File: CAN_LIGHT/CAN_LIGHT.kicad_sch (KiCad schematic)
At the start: 86 parts, among them IC1 MSPM0C1103SDDFR, J1 Conn_ARM_SWD_TagConnect_TC2030, J2 436500401, U1 TCAN334, U2 TPS76333DBVR

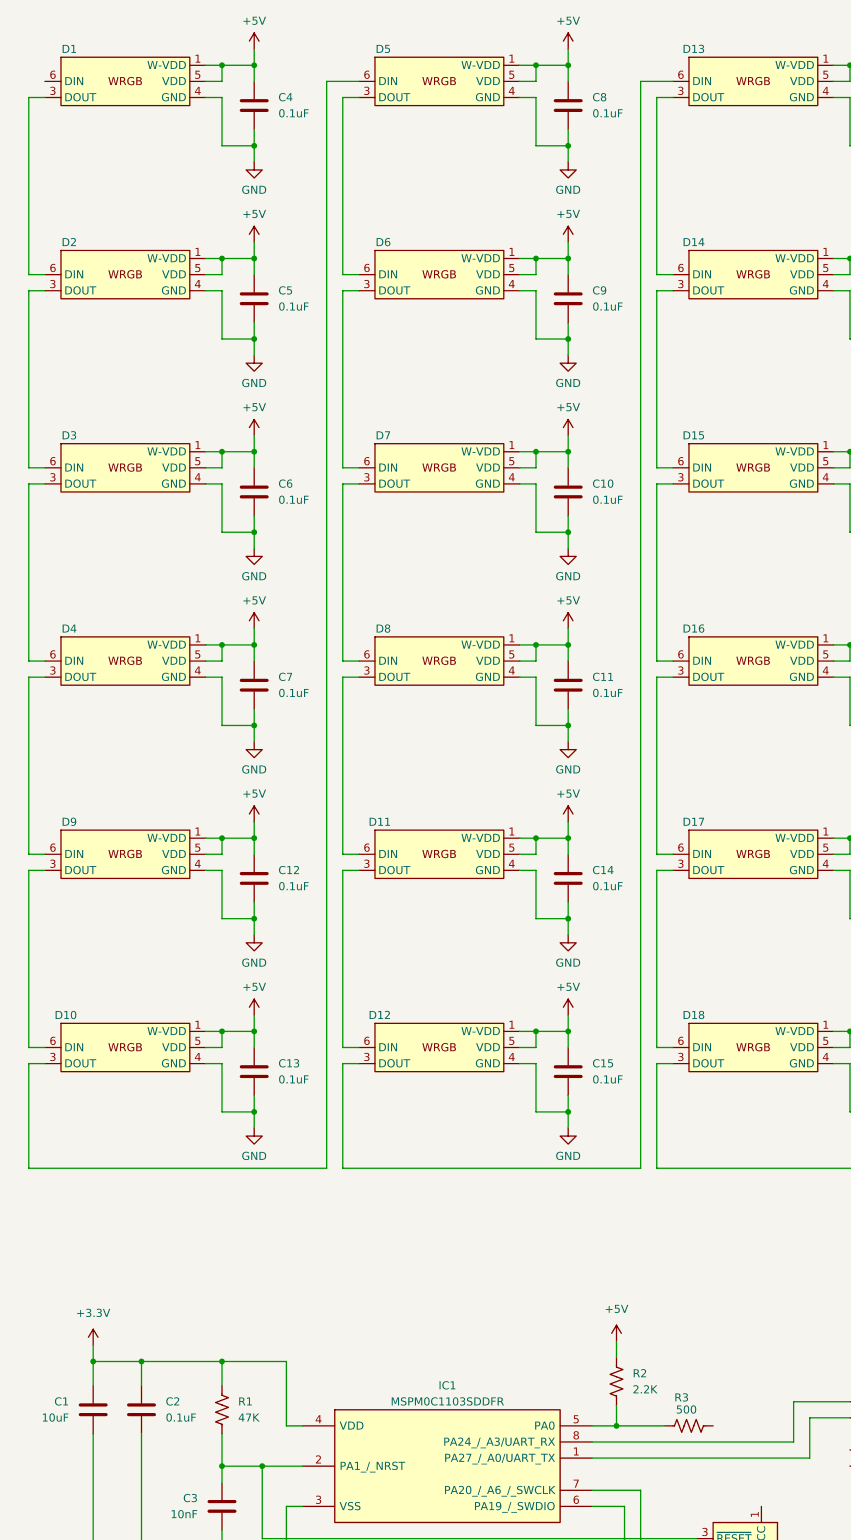
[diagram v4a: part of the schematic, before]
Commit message: Wire LEDs to MCU
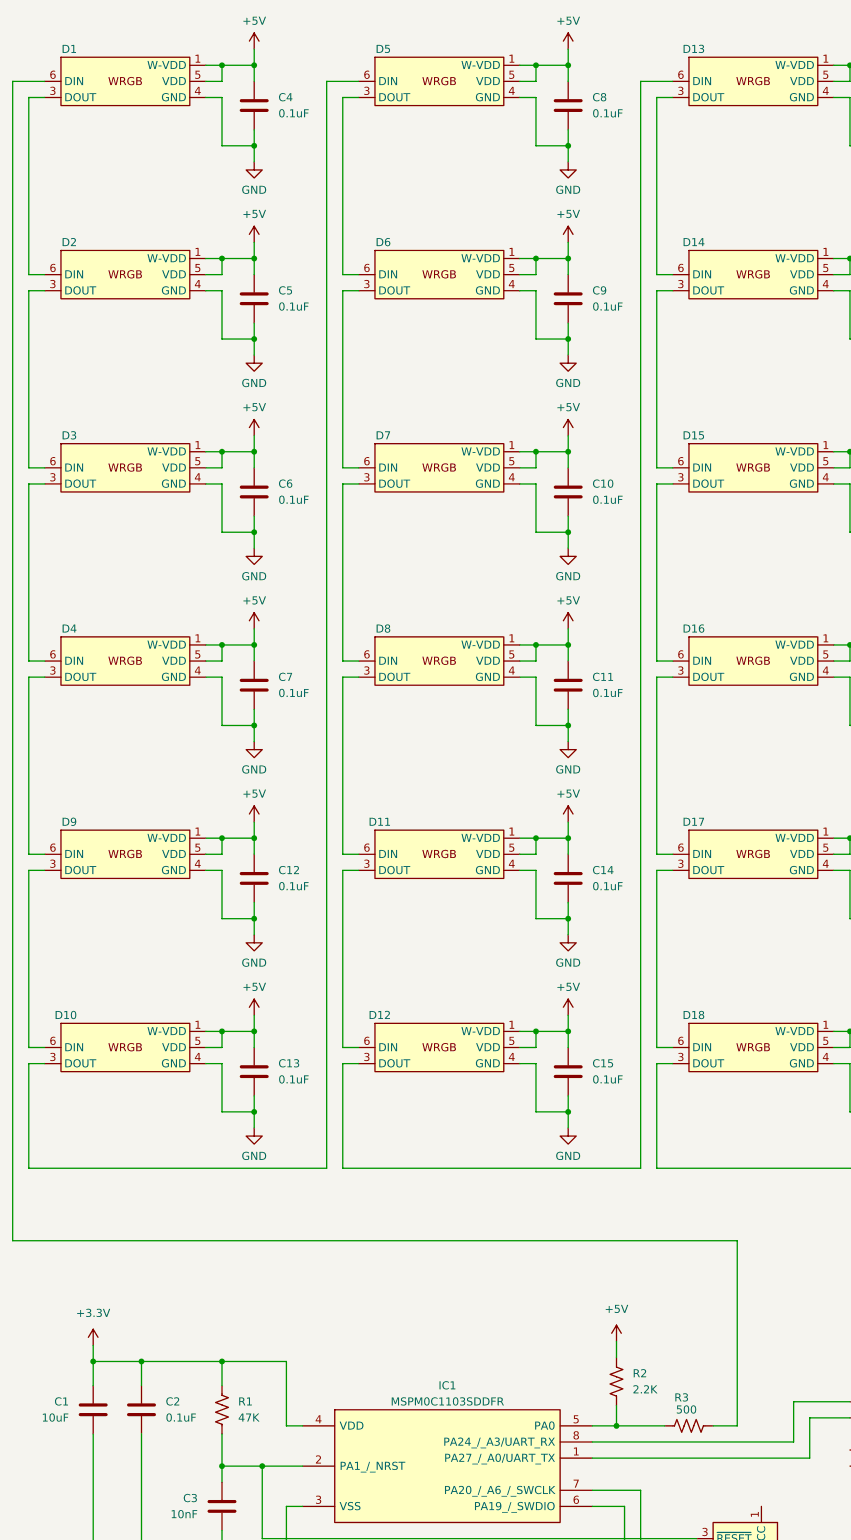
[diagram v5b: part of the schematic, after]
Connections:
- net at D1.6 (DIN): now also R3.2
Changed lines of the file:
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@@
+    (stroke (width 0) (type default))
+  )
+  (wire (pts (xy 127 236.22) (xy 130.81 236.22))
     (stroke (width 0) (type default))
   )
@@
     (stroke (width 0) (type default))
   )
+  (wire (pts (xy 130.81 236.22) (xy 130.81 207.01))
+    (stroke (width 0) (type default))
+  )
   (wire (pts (xy 104.14 143.51) (xy 99.06 143.51))
     (stroke (width 0) (type default))
@@
     (stroke (width 0) (type default))
   )
+  (wire (pts (xy 16.51 207.01) (xy 16.51 24.13))
+    (stroke (width 0) (type default))
+  )
   (wire (pts (xy 96.52 179.07) (xy 99.06 179.07))
     (stroke (width 0) (type default))
@@
     (stroke (width 0) (type default))
   )
+  (wire (pts (xy 16.51 24.13) (xy 21.59 24.13))
+    (stroke (width 0) (type default))
+  )
   (wire (pts (xy 203.2 186.69) (xy 203.2 189.23))
     (stroke (width 0) (type default))
@@
     (stroke (width 0) (type default))
   )
+  (wire (pts (xy 130.81 207.01) (xy 16.51 207.01))
+    (stroke (width 0) (type default))
+  )

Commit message: Add 12V to 5V buck converter
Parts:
- added U3: NCV891330PD50R2G, SOIC8_3P9X4P9_ONS, symbol NCV891330PD50R2G:NCV891330PD50R2G
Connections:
- net +12V: now also U3.1 (VIN)
- net +5V: now also U3.6 (VOUT)
- net GND: now also U3.4 (GND)
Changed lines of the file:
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@@
     (stroke (width 0) (type default))
   )
+  (wire (pts (xy 325.12 220.98) (xy 325.12 226.06))
+    (stroke (width 0) (type default))
+  )
   (wire (pts (xy 46.99 85.09) (xy 49.53 85.09))
     (stroke (width 0) (type default))
@@
     (stroke (width 0) (type default))
   )
+  (wire (pts (xy 386.08 218.44) (xy 386.08 208.28))
+    (stroke (width 0) (type default))
+  )
   (wire (pts (xy 124.46 254) (xy 55.88 254))
     (stroke (width 0) (type default))
@@
     (stroke (width 0) (type default))
   )
+  (wire (pts (xy 325.12 213.36) (xy 325.12 208.28))
+    (stroke (width 0) (type default))
+  )
   (wire (pts (xy 195.58 176.53) (xy 198.12 176.53))
     (stroke (width 0) (type default))
@@
     (stroke (width 0) (type default))
   )
+  (wire (pts (xy 330.2 213.36) (xy 325.12 213.36))
+    (stroke (width 0) (type default))
+  )
   (wire (pts (xy 252.73 140.97) (xy 252.73 143.51))
     (stroke (width 0) (type default))
@@
     (stroke (width 0) (type default))
   )
+  (wire (pts (xy 330.2 220.98) (xy 325.12 220.98))
+    (stroke (width 0) (type default))
+  )
   (wire (pts (xy 134.62 269.24) (xy 134.62 273.05))
     (stroke (width 0) (type default))
@@
     (stroke (width 0) (type default))
   )
+  (wire (pts (xy 370.84 218.44) (xy 386.08 218.44))
+    (stroke (width 0) (type default))
+  )
   (wire (pts (xy 153.67 113.03) (xy 153.67 115.57))
     (stroke (width 0) (type default))
@@
     )
   )
+  (symbol (lib_id "power:+5V") (at 386.08 208.28 0) (unit 1)
+    (in_bom yes) (on_board yes) (dnp no) (fields_autoplaced)
+    (property "Reference" "#PWR088" (at 386.08 212.09 0)
+      (effects (font (size 1.27 1.27)) hide)
+    )
+    (property "Value" "+5V" (at 386.08 203.2 0)
+      (effects (font (size 1.27 1.27)))
+    )
+    (property "Footprint" "" (at 386.08 208.28 0)
+      (effects (font (size 1.27 1.27)) hide)
+    )
+    (property "Datasheet" "" (at 386.08 208.28 0)
+      (effects (font (size 1.27 1.27)) hide)
+    )
+    (pin "1")
+    (instances
+      (project "CAN_LIGHT"
+        (path "/d4f25219-6cef-4e47-aded-6c41d03d24e2"
+          (reference "#PWR088") (unit 1)
+        )
+      )
+    )
+  )
   (symbol (lib_id "LED:IN-PI4818QAS5R5G5BPW") (at 24.13 27.94 0) (unit 1)
     (in_bom yes) (on_board yes) (dnp no)
@@
     )
   )
+  (symbol (lib_id "NCV891330PD50R2G:NCV891330PD50R2G") (at 330.2 213.36 0) (unit 1)
+    (in_bom yes) (on_board yes) (dnp no) (fields_autoplaced)
+    (property "Reference" "U3" (at 350.52 203.2 0)
+      (effects (font (size 1.524 1.524)))
+    )
+    (property "Value" "NCV891330PD50R2G" (at 350.52 205.74 0)
+      (effects (font (size 1.524 1.524)))
+    )
+    (property "Footprint" "SOIC8_3P9X4P9_ONS" (at 330.2 213.36 0)
+      (effects (font (size 1.27 1.27) italic) hide)
+    )
+    (property "Datasheet" "NCV891330PD50R2G" (at 330.2 213.36 0)
+      (effects (font (size 1.27 1.27) italic) hide)
+    )
+    (pin "1")
+    (pin "2")
+    (pin "3")
+    (pin "4")
+    (pin "5")
+    (pin "6")
+    (pin "7")
+    (pin "8")
+    (instances
+      (project "CAN_LIGHT"
+        (path "/d4f25219-6cef-4e47-aded-6c41d03d24e2"
+          (reference "U3") (unit 1)
+        )
+      )
+    )
+  )
   (symbol (lib_id "LED:IN-PI4818QAS5R5G5BPW") (at 271.78 180.34 0) (unit 1)
     (in_bom yes) (on_board yes) (dnp no)
@@
     )
   )
+  (symbol (lib_id "power:+12V") (at 325.12 208.28 0) (unit 1)
+    (in_bom yes) (on_board yes) (dnp no) (fields_autoplaced)
+    (property "Reference" "#PWR086" (at 325.12 212.09 0)
+      (effects (font (size 1.27 1.27)) hide)
+    )
+    (property "Value" "+12V" (at 325.12 203.2 0)
+      (effects (font (size 1.27 1.27)))
+    )
+    (property "Footprint" "" (at 325.12 208.28 0)
+      (effects (font (size 1.27 1.27)) hide)
+    )
+    (property "Datasheet" "" (at 325.12 208.28 0)
+      (effects (font (size 1.27 1.27)) hide)
+    )
+    (pin "1")
+    (instances
+      (project "CAN_LIGHT"
+        (path "/d4f25219-6cef-4e47-aded-6c41d03d24e2"
+          (reference "#PWR086") (unit 1)
+        )
+      )
+    )
+  )
   (symbol (lib_id "power:GND") (at 302.26 97.79 0) (mirror y) (unit 1)
     (in_bom yes) (on_board yes) (dnp no) (fields_autoplaced)
@@
         )
       )
+    )
+  )
+  (symbol (lib_id "power:GND") (at 325.12 226.06 0) (unit 1)
+    (in_bom yes) (on_board yes) (dnp no) (fields_autoplaced)
+    (property "Reference" "#PWR087" (at 325.12 232.41 0)
+      (effects (font (size 1.27 1.27)) hide)
+    )
+    (property "Value" "GND" (at 325.12 231.14 0)
+      (effects (font (size 1.27 1.27)))
+    )
+    (property "Footprint" "" (at 325.12 226.06 0)
+      (effects (font (size 1.27 1.27)) hide)
+    )
+    (property "Datasheet" "" (at 325.12 226.06 0)
+      (effects (font (size 1.27 1.27)) hide)
+    )
+    (pin "1")
+    (instances
+      (project "CAN_LIGHT"
+        (path "/d4f25219-6cef-4e47-aded-6c41d03d24e2"
+          (reference "#PWR087") (unit 1)
+        )
+      )

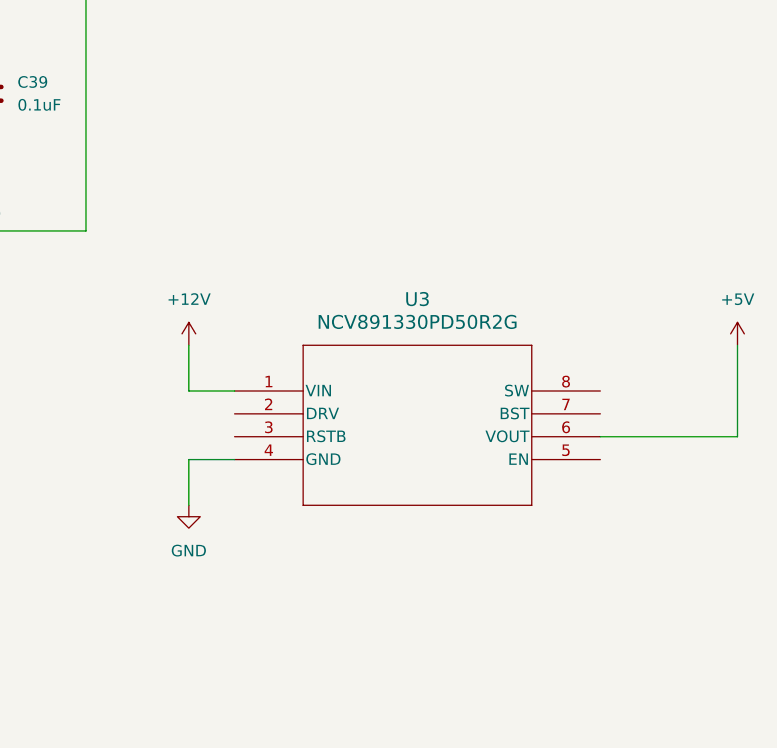
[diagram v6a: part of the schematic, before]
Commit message: Import initial PCB shape and roughly place LEDs on perimeter
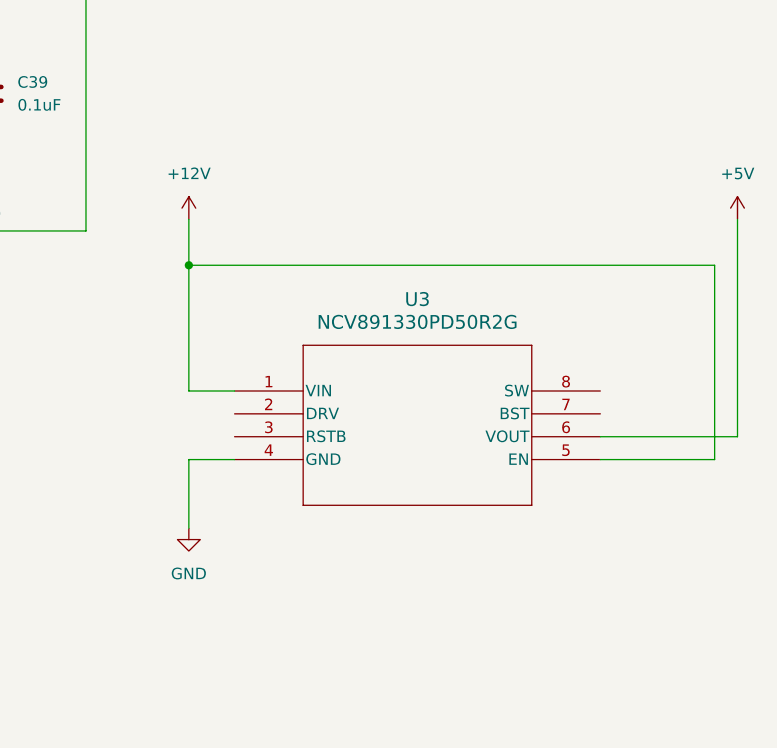
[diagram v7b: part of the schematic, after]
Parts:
- D1, D10, D11, D12, D13, D14, D15, D16, D17, D18, D19, D2, D20, D21, D22, D23, D24, D25, D26, D27, D28, D29, D3, D30, D31, D32, D33, D34, D35, D36, D4, D5, D6, D7, D8, D9: footprint (none) -> IN-PI4818QAS5R5G5BPW:INPI4818QAS5R5G5BPW
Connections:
- net +12V: now also U3.5 (EN)

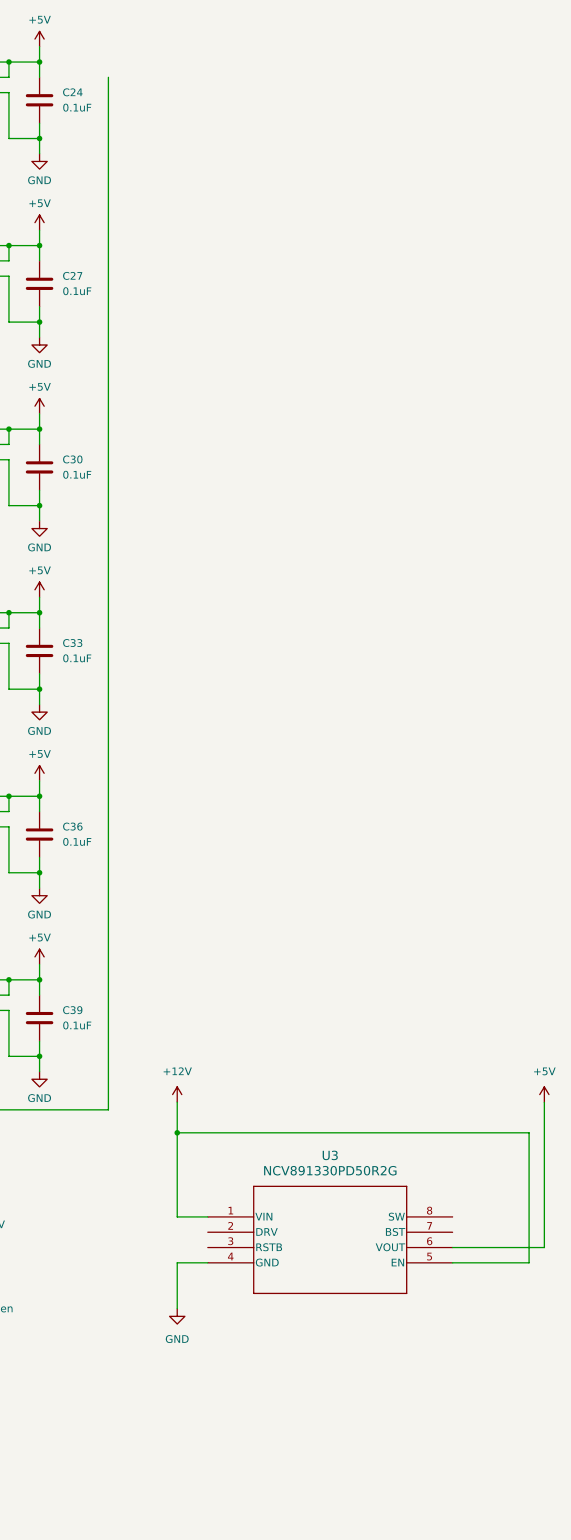
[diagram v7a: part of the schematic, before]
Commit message: Move LEDs to outside of curve, add 5 more to fill out outline
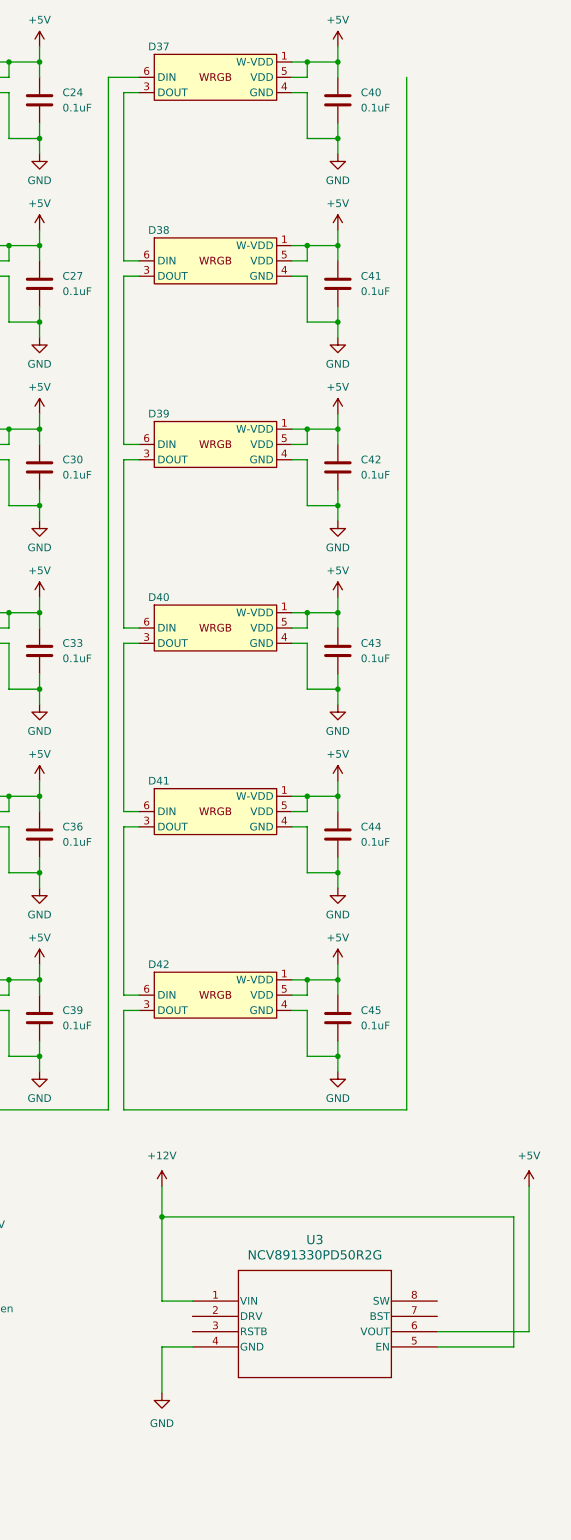
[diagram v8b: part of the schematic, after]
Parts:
- added C40, C41, C42, C43, C44, C45: 0.1uF, Capacitor_SMD:C_0603_1608Metric_Pad1.08x0.95mm_HandSolder, symbol Device:C
- added D37, D38, D39, D40, D41, D42: ~, IN-PI4818QAS5R5G5BPW:INPI4818QAS5R5G5BPW, symbol LED:IN-PI4818QAS5R5G5BPW
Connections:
- net +5V: now also C40.1, C41.1, C42.1, C43.1, C44.1, C45.1, D37.1 (W-VDD), D37.5 (VDD), D38.1 (W-VDD), D38.5 (VDD), D39.1 (W-VDD), D39.5 (VDD), D40.1 (W-VDD), D40.5 (VDD), D41.1 (W-VDD), D41.5 (VDD), D42.1 (W-VDD), D42.5 (VDD)
- net GND: now also C40.2, C41.2, C42.2, C43.2, C44.2, C45.2, D37.4 (GND), D38.4 (GND), D39.4 (GND), D40.4 (GND), D41.4 (GND), D42.4 (GND)
- net at D36.3 (DOUT): now also D37.6 (DIN)
- new net: D37.3 (DOUT), D38.6 (DIN)
- new net: D41.3 (DOUT), D42.6 (DIN)
- new net: D39.3 (DOUT), D40.6 (DIN)
- new net: D38.3 (DOUT), D39.6 (DIN)
- new net: D40.3 (DOUT), D41.6 (DIN)
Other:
- moved on the sheet: U3
